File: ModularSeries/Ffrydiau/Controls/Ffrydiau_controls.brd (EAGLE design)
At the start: 100 x 49 mm, 91 parts, among them IC3 556_DUALTIMERDIL14, Q1 2N3906, Q2 2N3904, Q3 2N3904, Q4 2N7000, Q5 2N7000, Q6 2N3904, Q7 2N3904, SW1 3XWIREPAD

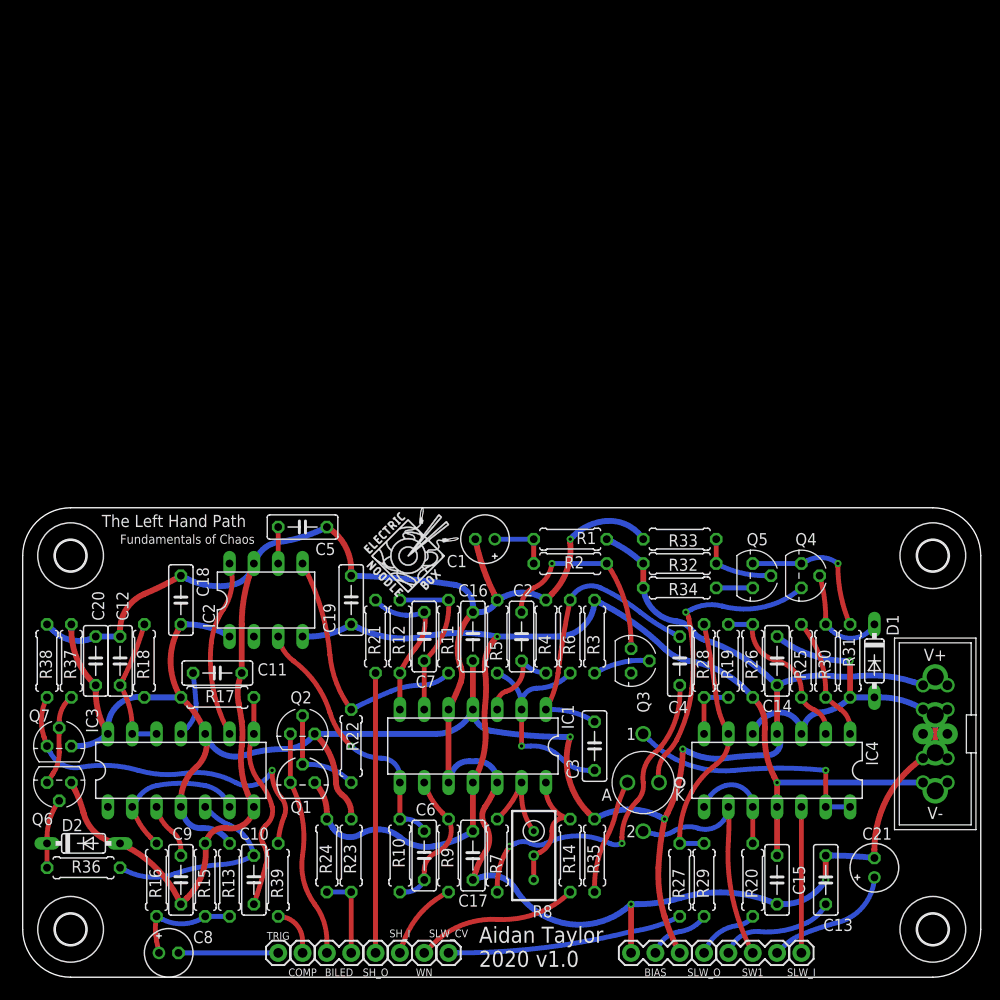
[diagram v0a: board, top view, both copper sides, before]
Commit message: Portals BOM update, Ffrydiau project added
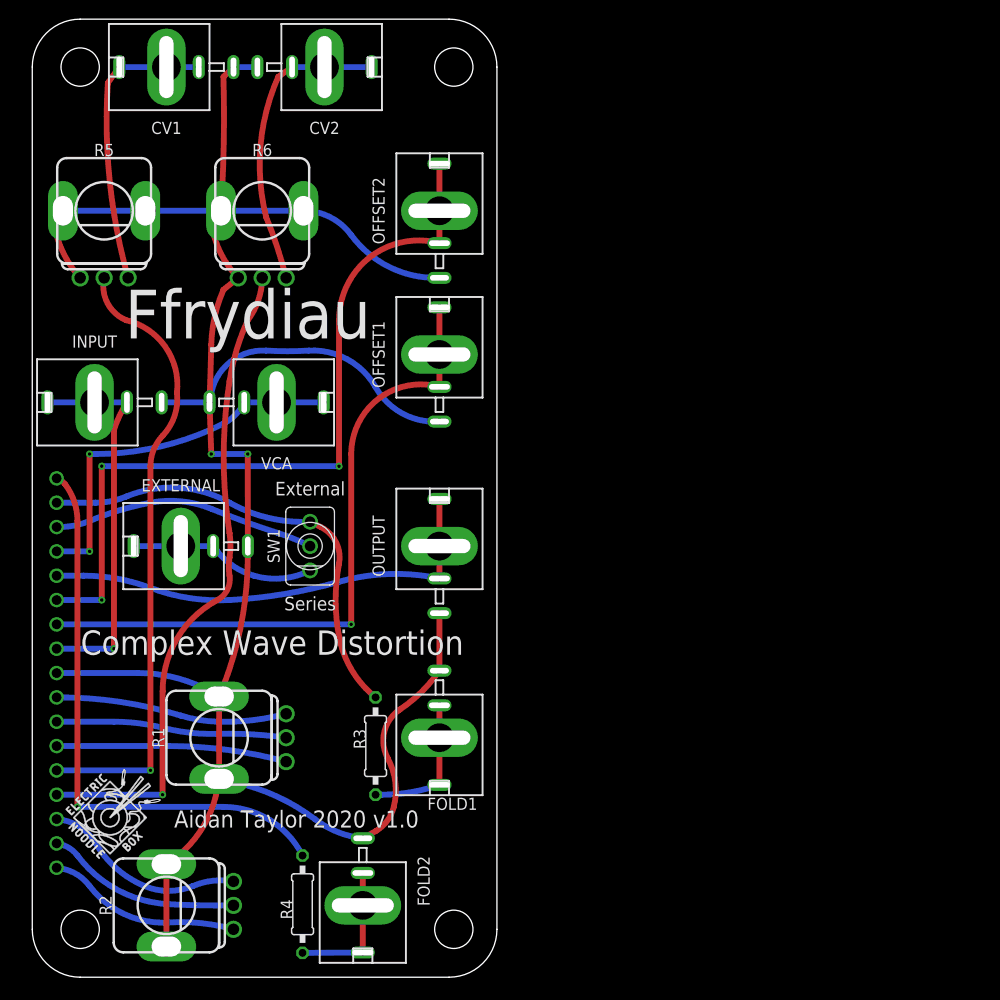
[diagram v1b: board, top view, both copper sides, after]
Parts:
- removed BIAS: 3XWIREPAD, ElectricNoodleBox:1X03
- removed BILED: 2XWIREPAD, ElectricNoodleBox:1X02
- removed C1: 1µF, rcl:E2-5
- removed C10: 2.2nF, rcl:C050-025X075
- removed C11, C9: 10nF, rcl:C050-025X075
- removed C12, C14, C15, C16, C17, C18, C19, C2, C20, C4: 100nF, rcl:C050-025X075
- removed C13, C6: 22pF, rcl:C050-025X075
- removed C21: BP 4.7µF, rcl:E2-5
- removed C3: 10pF, rcl:C050-025X075
- removed C5: 47nF, rcl:C050-025X075
- removed C7: 15pF, rcl:C050-025X075
- removed C8: 4.7µF, rcl:E2-5
- removed COMP, SH_I, SH_O, SLW_CV, SLW_I, SLW_O, TRIG, WN: 1XWIREPAD, ElectricNoodleBox:1X01
- removed D1, D2: BAT85, ElectricNoodleBox:DO35-7
- removed H1, H2, H3, H4: MOUNT-HOLE3.2, holes:3,2
- removed IC1, IC4: (no value), ElectricNoodleBox:DIL14
- removed IC2: (no value), ElectricNoodleBox:DIL08
- removed IC3: 556_DUALTIMERDIL14, ElectricNoodleBox:DIL14
- removed OC1: OPTOCOUPLERSILONEX, ElectricNoodleBox:SILONEX_OPTOCOUPLER
- removed Q1: 2N3906, transistor-pnp:TO92
- removed Q2, Q3, Q6, Q7: 2N3904, transistor:TO92
- removed Q4, Q5: 2N7000, ElectricNoodleBox:TO92
- removed R10, R16, R19, R22, R25, R30, R31, R9: 10K, rcl:0207/7
- removed R11, R12, R18, R7: 1K, rcl:0207/7
- removed R13, R15, R27, R28, R29: 100K, rcl:0207/7
- removed R14, R20, R21: 100Ω, rcl:0207/7
- removed R17: 20K, rcl:0207/7
- removed R23, R24, R34, R35: 4K7, rcl:0207/7
- removed R26, R32: 47K, rcl:0207/7
- removed R33, R36, R37: 15K, rcl:0207/7
- removed R38: 470Ω, rcl:0207/7
- removed R39: 220Ω, rcl:0207/7
- removed R8: 100K, rcl:RTRIM3296W
- removed WP1: COMBO_SUPPLY_HEADER, ElectricNoodleBox:COMBINED_POWER
- added BOARD1: FFRYDIAU_LINK, ElectricNoodleBox:FFRYDIAU
- added CV1, CV2, EXTERNAL, FOLD1, FOLD2, INPUT, OFFSET1, OFFSET2, OUTPUT, VCA: COMBI-JACKCINCHNANA, ElectricNoodleBox:NEWCOMBOJACK_PANEL
- added U$2: (no value), ElectricNoodleBox:LOGO10X10
- R1, R2, R6: value 470K -> B100K; device rcl:0207/7 -> ElectricNoodleBox:ALPHA_RV09_9MMPOT
- R3: value 10K -> 100Ω; device rcl:0207/7 -> rcl:0207/10
- R4: value 2M -> 100Ω; device rcl:0207/7 -> rcl:0207/10
- R5: value 10K -> B100K; device rcl:0207/7 -> ElectricNoodleBox:ALPHA_RV09_9MMPOT
- SW1: value 3XWIREPAD -> SPDT_SWITCHDW1; device ElectricNoodleBox:1X03 -> ElectricNoodleBox:MICRODPDT-DW1
- moved SW1 60.9 mm to (30.0, 45.0), turned to 180 degrees
- moved R5 60.5 mm to (8.50, 80.0), turned to 0 degrees
- moved R2 55.2 mm to (15.0, 7.50), turned to 90 degrees
- moved R6 54.9 mm to (25.0, 80.0), turned to 0 degrees
- moved R1 42.1 mm to (20.5, 25.0), turned to 90 degrees
- moved U$1 41.4 mm to (4.45, 12.1)
- moved R4 37.8 mm to (29.2, 7.62), turned to 270 degrees
- moved R3 25.6 mm to (36.8, 24.1), turned to 270 degrees
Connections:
- removed net +12V: BIAS.3, C14.2, C16.2, C18.2, C20.2, IC1.4, IC2.1, IC3.10, IC3.14, IC3.4, IC4.4, Q2.1, Q7.1, R1.2, R13.1, R17.1, R18.1, R23.2, R32.2, R34.2, R35.2, R37.2, WP1.V+1, WP1.V+2, WP1.V+3
- removed net -12V: C15.1, C17.1, C19.1, IC1.11, IC2.4, IC4.11, Q1.1, R24.1, R26.1, R3.2, WP1.V-1, WP1.V-2, WP1.V-3
- removed net N$18: C8.+, R13.2, R15.1, R16.1
- removed net N$23: C11.2, IC3.11
- removed net N$24: C12.2, IC3.12, IC3.13, R18.2
- removed net N$25: IC2.8, IC3.9
- removed net N$26: C8.-, TRIG.1
- removed net N$27: IC4.12, SLW_I.1
- removed net N$28: IC4.13, IC4.14, OC1.1
- removed net N$29: IC4.7, R19.1, R28.2
- removed net N$30: IC4.9, OC1.2, SW1.2
- removed net N$31: IC4.10, IC4.8, R20.1
- removed net N$32: R20.2, SLW_O.1
- removed net N$33: R21.2, SH_O.1
- removed net N$34: Q1.2, Q2.2, R22.2
- removed net N$35: BILED.2, Q1.3, Q2.3
- removed net N$36: BILED.1, R23.1, R24.2
- removed net N$37: IC4.2, R19.2, R25.1, R26.2
- removed net N$38: IC4.6, R27.2, R28.1, R29.2
- removed net N$39: IC4.1, R25.2, R30.1
- removed net N$40: D1.C, Q4.2, R30.2
- removed net N$41: Q4.1, Q5.1, R31.2
- removed net N$42: C21.+, SW1.3
- removed net N$43: Q5.2, R32.1, R33.2
- removed net N$44: Q5.3, R34.1
- removed net N$45: OC1.A, R35.1
- removed net N$46: C13.2, SW1.1
- removed net N$47: R27.1, SLW_CV.1
- removed net N$48: BIAS.2, R29.1
- removed net N$49: Q6.1, Q7.2, R37.1
- removed net N$50: Q7.3, R38.2, R39.1
- removed net N$51: COMP.1, R39.2
- removed net N$52: D2.C, Q6.2, R36.1
- removed net OPTO_KATHODE: OC1.K, Q4.3
- net AGND: now also BOARD1.GND, CV1.S, CV2.S, EXTERNAL.S, FOLD1.S, FOLD2.S, INPUT.S, OFFSET1.S, OFFSET2.S, OUTPUT.S, R1.LUGL, R1.LUGR, R2.LUGL, R2.LUGR, R5.C1, R5.LUGL, R5.LUGR, R6.C1, R6.LUGL, R6.LUGR, VCA.S; no longer BIAS.1, C1.-, C11.1, C12.1, C13.1, C14.1, C15.2, C16.1, C17.2, C18.1, C19.2, C20.1, C21.-, C5.1, C9.1, D1.A, D2.A, IC1.10, IC1.12, IC1.5, IC2.7, IC3.7, IC4.3, IC4.5, Q6.3, R15.2, R31.1, R33.1, R38.1, R4.2, R5.2, WP1.GND1, WP1.GND2, WP1.GND3, WP1.GND4, WP1.GND5, WP1.GND6, WP1.GND7, WP1.GND8
- net N$1: now also CV1.CONN, CV1.T1, CV1.T2, R5.C3; no longer C1.+, R1.1, R2.2
- net N$10: now also BOARD1.POT1_3, R1.C3; no longer C6.1, IC1.9, R10.1, R9.2
- net N$11: now also BOARD1.POT2_2, R2.C2; no longer C6.2, IC1.8, IC2.3, R10.2
- net N$12: now also BOARD1.POT2_3, R2.C3; no longer C5.2, IC2.6
- net N$13: now also BOARD1.POT2_1, R2.C1; no longer IC2.5, R11.1, R22.1
- net N$14: now also BOARD1.SWITCH_S, R3.1, SW1.C1; no longer C7.1, IC1.6, R11.2, R12.1
- net N$15: now also FOLD1.CONN, FOLD1.T1, FOLD1.T2, R3.2; no longer C7.2, IC1.7, R12.2, R21.1
- net N$16: now also BOARD1.SWITCH_R, SW1.C2; no longer R9.1, SH_I.1
- net N$17: now also EXTERNAL.CONN, EXTERNAL.T1, EXTERNAL.T2, SW1.C3; no longer C10.2, IC3.5, R36.2
- net N$19: now also BOARD1.FOLD2, R4.1; no longer IC3.2, IC3.6, R16.2
- net N$2: now also BOARD1.CV1, R5.C2; no longer C2.1, Q3.3, R2.1
- net N$20: now also FOLD2.CONN, FOLD2.T1, FOLD2.T2, R4.2; no longer R14.2, WN.1
- net N$21: now also CV2.CONN, CV2.T1, CV2.T2, R6.C3; no longer C9.2, IC3.3
- net N$22: now also BOARD1.CV2, R6.C2; no longer C10.1, IC3.8, R17.2
- net N$3: now also BOARD1.SIG, INPUT.CONN, INPUT.T1, INPUT.T2; no longer Q3.2, R3.1
- net N$4: now also BOARD1.OUT, OUTPUT.CONN, OUTPUT.T1, OUTPUT.T2; no longer C2.2, IC1.3, R4.1
- net N$5: now also BOARD1.POT1_2, R1.C2; no longer C3.1, IC1.2, R5.1, R6.1
- net N$6: now also BOARD1.OFS1, OFFSET1.CONN, OFFSET1.T1, OFFSET1.T2; no longer C3.2, C4.1, IC1.1, R6.2
- net N$7: now also BOARD1.OFS2, OFFSET2.CONN, OFFSET2.T1, OFFSET2.T2; no longer C4.2, R7.1
- net N$8: now also BOARD1.VCA, VCA.CONN, VCA.T1, VCA.T2; no longer IC1.13, R7.2, R8.1
- net N$9: now also BOARD1.POT1_1, R1.C1; no longer IC1.14, R14.1, R8.2, R8.3
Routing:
- net +12V: track 211.5 -> 0.00 mm, vias 3 -> 0
- net -12V: track 128.1 -> 0.00 mm, vias 2 -> 0
- net AGND: track 294.7 -> 245.3 mm, vias 4 -> 2
- net N$7: track 34.5 -> 80.2 mm, vias 2 -> 3
- net N$22: track 22.3 -> 67.4 mm, vias 0 -> 1
- net N$19: track 16.5 -> 60.6 mm, vias 0 -> 1
- net N$2: track 21.1 -> 63.9 mm
- net N$4: track 8.64 -> 48.6 mm
- net N$6: track 30.1 -> 68.4 mm, vias 0 -> 1
- net N$50: track 37.6 -> 0.00 mm, vias 1 -> 0
- net N$3: track 5.93 -> 40.3 mm, vias 0 -> 1
- net OPTO_KATHODE: track 31.0 -> 0.00 mm, vias 1 -> 0
- net N$14: track 17.0 -> 47.3 mm
- net N$8: track 9.87 -> 39.3 mm, vias 0 -> 2
- net N$33: track 29.2 -> 0.00 mm
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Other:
- board size 100 x 49 mm -> 48.5 x 100 mm
- board text added: "Complex Wave Distortion"
- board text added: "External"
- board text added: "Ffrydiau"
- board text added: "Series"
- board text removed: "Fundamentals of Chaos"
- board text removed: "The Left Hand Path"

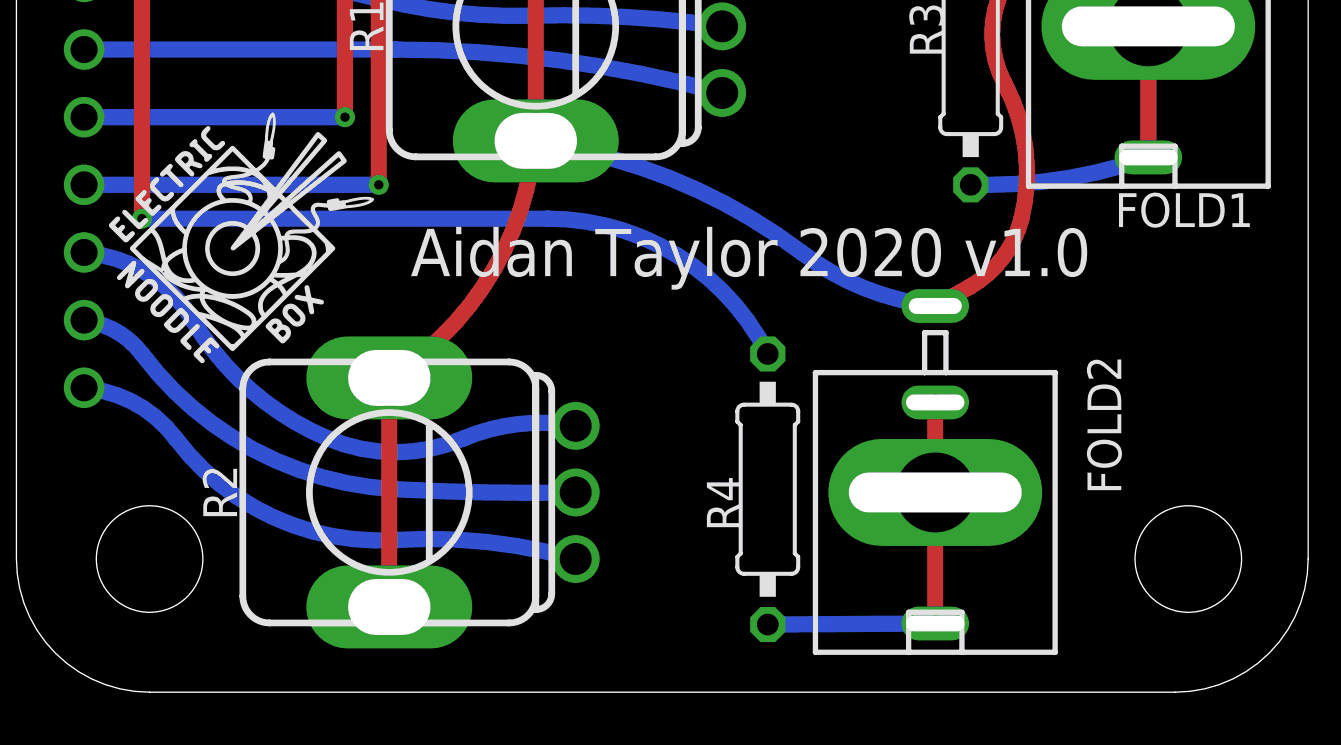
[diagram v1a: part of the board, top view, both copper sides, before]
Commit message: Layout and schematic renders for LHP added
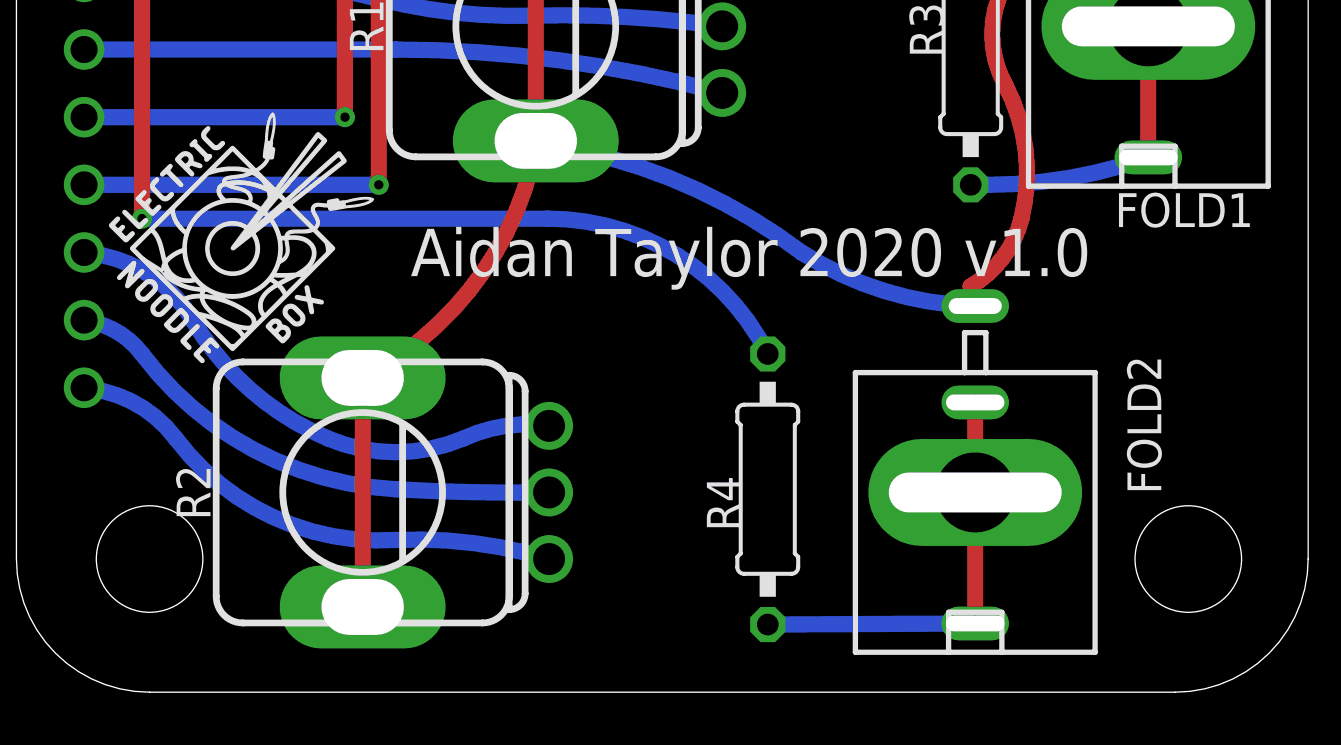
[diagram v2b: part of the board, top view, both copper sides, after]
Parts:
- moved FOLD2 1.50 mm to (37.0, 7.50)
- moved R2 1.00 mm to (14.0, 7.50)
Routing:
- net N$20: track 14.6 -> 16.1 mm
- net AGND: track 245.3 -> 246.5 mm
- net N$11: track 20.8 -> 19.8 mm
- net N$13: track 20.5 -> 19.5 mm
- net N$12: track 21.6 -> 20.6 mm
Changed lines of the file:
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@@
 </layers>
 <board>
+<fusionsync huburn="a.cGVyc29uYWw6dWUyYjdlNGE0" projecturn="a.cGVyc29uYWw6dWUyYjdlNGE0IzIwMjAwNDA1MjgzMzA0MTgx" f3durn="urn:adsk.wipprod:dm.lineage:U52Gq_qCSYWslIBvySlGKA" pcbguid="ab27ca16-c39a-4c1f-a0a6-96c191041e3a" lastpulledtime="" lastsyncedchangeguid="" latestrevisionid="5210aafa-dc9b-4d78-86f5-985a4f60700b" lastsyncedrevisionid="5210aafa-dc9b-4d78-86f5-985a4f60700b" lastboardhashguid="bbd2f230-9539-75b5-5f75-3093f009b13a" lastpushedtime="2020-07-16T15:12:55Z" linktopcb3d="true"/>
 <plain>
 <text x="30" y="39" size="1.4224" layer="21" font="vector" align="center">Series</text>
@@
 <attribute name="NAME" x="7.5" y="66.35" size="1.27" layer="25" font="vector" rot="R180" align="center"/>
 </element>
-<element name="FOLD2" library="ElectricNoodleBox" package="NEWCOMBOJACK_PANEL" value="COMBI-JACKCINCHNANA" x="35.5" y="7.5" smashed="yes" rot="R180">
-<attribute name="NAME" x="41.85" y="10.04" size="1.27" layer="25" font="vector" rot="R270" align="center"/>
+<element name="FOLD2" library="ElectricNoodleBox" package="NEWCOMBOJACK_PANEL" value="COMBI-JACKCINCHNANA" x="37" y="7.5" smashed="yes" rot="R180">
+<attribute name="NAME" x="43.35" y="10.04" size="1.27" layer="25" font="vector" rot="R270" align="center"/>
 </element>
 <element name="OFFSET1" library="ElectricNoodleBox" package="NEWCOMBOJACK_PANEL" value="COMBI-JACKCINCHNANA" x="43.5" y="65" smashed="yes">
@@
 <attribute name="VALUE" x="28.12" y="32.62" size="1.27" layer="27" rot="R90" align="center"/>
 </element>
-<element name="R2" library="ElectricNoodleBox" package="ALPHA_RV09_9MMPOT" value="B100K" x="15" y="7.5" smashed="yes" rot="R90">
-<attribute name="NAME" x="8.65" y="7.5" size="1.27" layer="25" rot="R90" align="center"/>
-<attribute name="VALUE" x="22.62" y="15.12" size="1.27" layer="27" rot="R90" align="center"/>
+<element name="R2" library="ElectricNoodleBox" package="ALPHA_RV09_9MMPOT" value="B100K" x="14" y="7.5" smashed="yes" rot="R90">
+<attribute name="NAME" x="7.65" y="7.5" size="1.27" layer="25" rot="R90" align="center"/>
+<attribute name="VALUE" x="21.62" y="15.12" size="1.27" layer="27" rot="R90" align="center"/>
 </element>
 <element name="R3" library="rcl" library_urn="urn:adsk.eagle:library:334" package="0207/10" package3d_urn="urn:adsk.eagle:package:23491/2" value="100Ω" x="36.83" y="24.13" smashed="yes" rot="R270">
@@
 <wire x1="43.5" y1="38" x2="43.5" y2="32" width="0.6096" layer="1"/>
 <wire x1="20.5" y1="29.3" x2="20.5" y2="20.7" width="0.6096" layer="1"/>
-<wire x1="35.5" y1="14.5" x2="36.83" y2="15.24" width="0.6096" layer="1"/>
+<wire x1="37" y1="14.5" x2="36.83" y2="15.24" width="0.6096" layer="1"/>
 <wire x1="36.83" y1="15.24" x2="38.735" y2="17.78" width="0.6096" layer="1" curve="45.803444"/>
 <wire x1="38.735" y1="17.78" x2="38.1" y2="22.86" width="0.6096" layer="1" curve="42.186399"/>
@@
 <wire x1="20.5" y1="20.7" x2="22.225" y2="20.32" width="0.6096" layer="16"/>
 <wire x1="22.225" y1="20.32" x2="30.48" y2="16.51" width="0.6096" layer="16" curve="-24.703763"/>
-<wire x1="30.48" y1="16.51" x2="35.5" y2="14.5" width="0.6096" layer="16" curve="31.079693"/>
+<wire x1="30.48" y1="16.51" x2="37" y2="14.5" width="0.6096" layer="16" curve="31.079693"/>
 <wire x1="20.5" y1="20.7" x2="20.32" y2="19.685" width="0.6096" layer="1"/>
-<wire x1="20.32" y1="19.685" x2="15" y2="11.8" width="0.6096" layer="1" curve="-47.902436"/>
-<wire x1="15" y1="11.8" x2="15" y2="3.2" width="0.6096" layer="1"/>
+<wire x1="20.32" y1="19.685" x2="14" y2="11.8" width="0.6096" layer="1" curve="-47.902436"/>
+<wire x1="14" y1="11.8" x2="14" y2="3.2" width="0.6096" layer="1"/>
 </signal>
 <signal name="N$5">
@@
 <wire x1="3.175" y1="13.97" x2="5.715" y2="12.7" width="0.6096" layer="16" curve="-53.130102"/>
 <wire x1="5.715" y1="12.7" x2="15.24" y2="7.62" width="0.6096" layer="16" curve="50.115227"/>
-<wire x1="15.24" y1="7.62" x2="22" y2="7.5" width="0.6096" layer="16" curve="3.995769"/>
+<wire x1="15.24" y1="7.62" x2="21" y2="7.5" width="0.6096" layer="16" curve="3.995769"/>
 </signal>
 <signal name="N$12">
@@
 <wire x1="7.62" y1="13.97" x2="12.7" y2="9.525" width="0.6096" layer="16" curve="36.607676"/>
 <wire x1="12.7" y1="9.525" x2="17.78" y2="9.525" width="0.6096" layer="16" curve="45.764186"/>
-<wire x1="17.78" y1="9.525" x2="22" y2="10" width="0.6096" layer="16" curve="-32.919911"/>
+<wire x1="17.78" y1="9.525" x2="21" y2="10" width="0.6096" layer="16" curve="-32.919911"/>
 </signal>
 <signal name="N$13">
@@
 <wire x1="3.175" y1="11.43" x2="6.985" y2="9.525" width="0.6096" layer="16" curve="-53.130102"/>
 <wire x1="6.985" y1="9.525" x2="15.24" y2="5.715" width="0.6096" layer="16" curve="56.709918"/>
-<wire x1="15.24" y1="5.715" x2="22" y2="5" width="0.6096" layer="16" curve="-19.235004"/>
+<wire x1="15.24" y1="5.715" x2="21" y2="5" width="0.6096" layer="16" curve="-19.235004"/>
 </signal>
 <signal name="N$14">
@@
 <contactref element="FOLD2" pad="T1"/>
 <contactref element="FOLD2" pad="T2"/>
-<wire x1="35.5" y1="10.88" x2="35.5" y2="7.5" width="0.6096" layer="1"/>
-<wire x1="35.5" y1="7.5" x2="35.5" y2="2.58" width="0.6096" layer="1"/>
-<wire x1="29.21" y1="2.54" x2="35.5" y2="2.58" width="0.6096" layer="16"/>
+<wire x1="37" y1="10.88" x2="37" y2="7.5" width="0.6096" layer="1"/>
+<wire x1="37" y1="7.5" x2="37" y2="2.58" width="0.6096" layer="1"/>
+<wire x1="29.21" y1="2.54" x2="37" y2="2.58" width="0.6096" layer="16"/>
 </signal>
 <signal name="N$1">
@@
 </note>
 <note version="8.3" severity="warning">
+Since Version 8.3, EAGLE supports Fusion synchronisation.
+This feature will not be available in this version and saving
+the document will break the link to the Fusion PCB feature.
+</note>
+<note version="8.3" severity="warning">
